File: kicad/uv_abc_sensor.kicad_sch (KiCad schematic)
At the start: 19 parts, among them J1 Conn_01x04, J2 Conn_01x04, Q1 BSS138, Q2 BSS138, U1 AS7331, U2 AP2112K-3.3

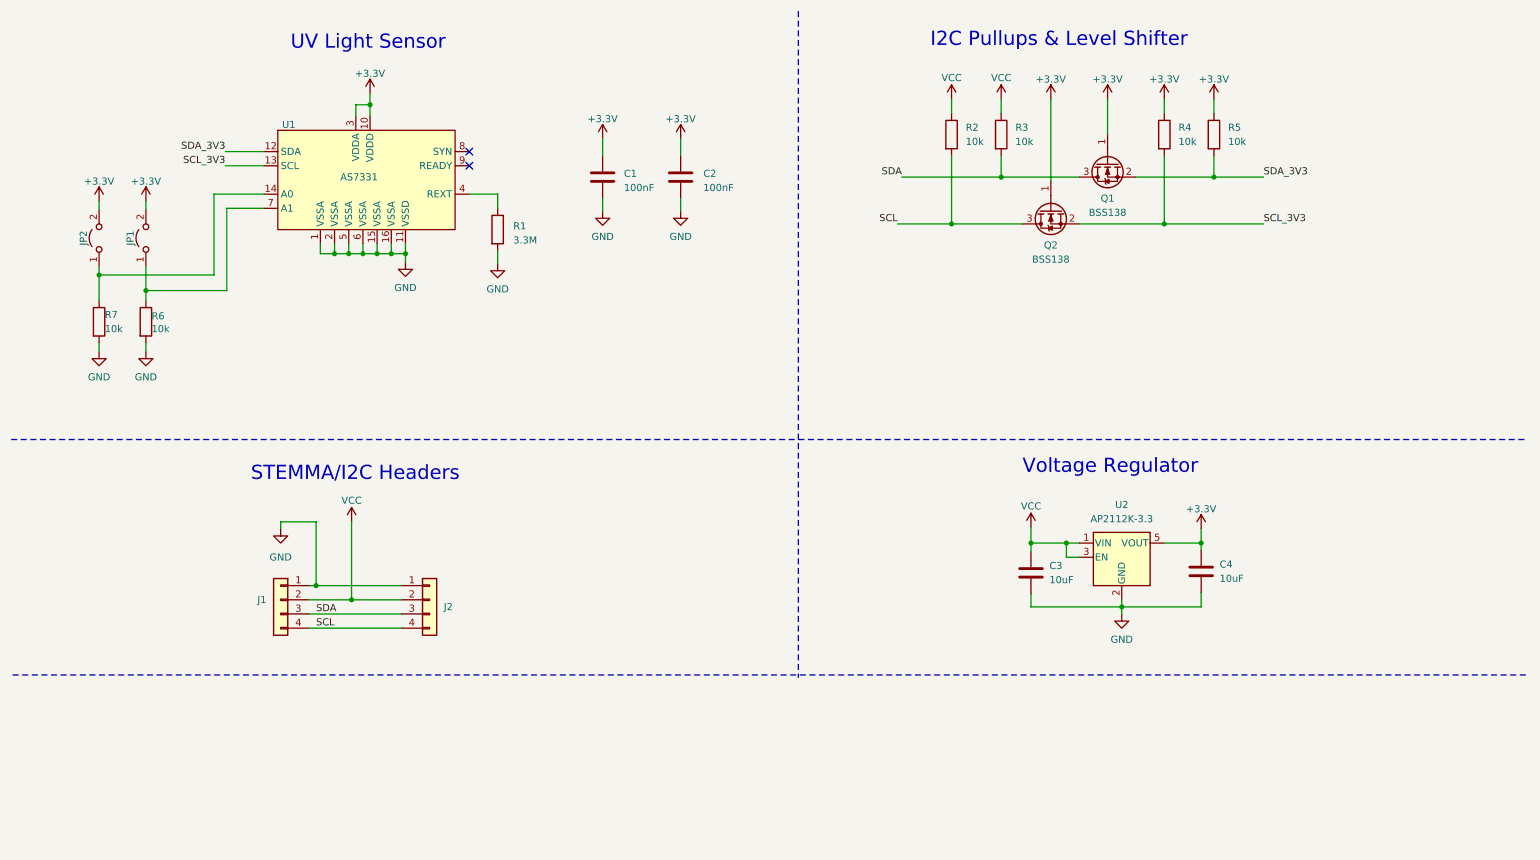
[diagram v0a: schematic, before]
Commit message: Worked on footprint assignment and PCB layout.
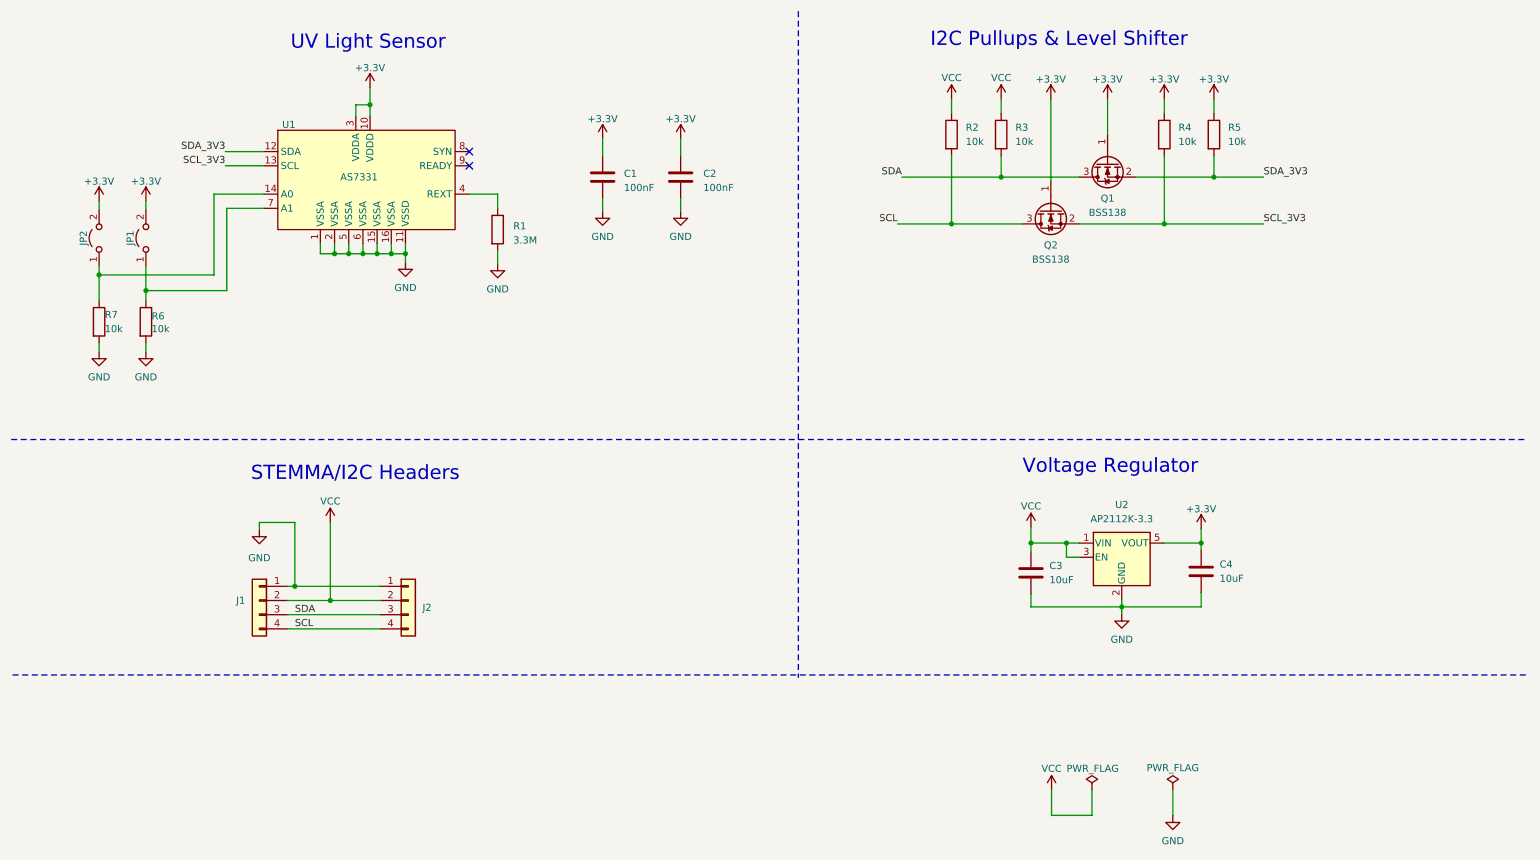
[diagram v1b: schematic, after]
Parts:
- C1, C2, C3, C4: footprint (none) -> Capacitor_SMD:C_0402_1005Metric
- J1, J2: footprint (none) -> BOOMELE_SH_SMD:BOOMELE_SMD_SH_4PIN_RT
- JP1, JP2: footprint (none) -> Jumper:SolderJumper-2_P1.3mm_Open_TrianglePad1.0x1.5mm
- R1, R2, R3, R4, R5, R6, R7: footprint (none) -> Resistor_SMD:R_0402_1005Metric
- U1: footprint (none) -> AS7331:AS7331
